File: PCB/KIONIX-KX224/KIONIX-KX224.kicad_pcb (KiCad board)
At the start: 2 copper layers, 7 parts, among them J1 Conn_02x03_Odd_Even

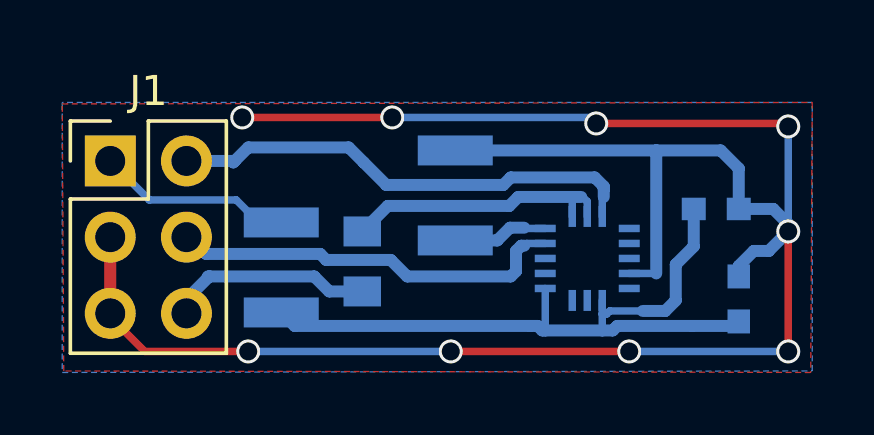
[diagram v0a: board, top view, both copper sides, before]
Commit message: PCB - KX224 update to have file conform to manufacturate PCB
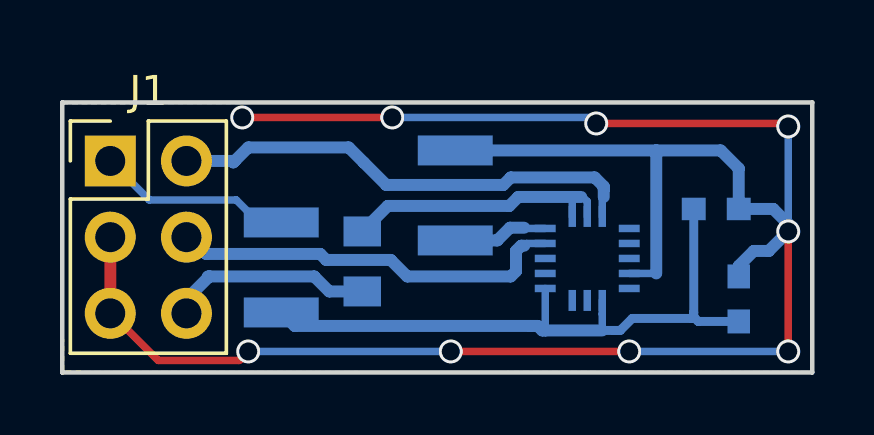
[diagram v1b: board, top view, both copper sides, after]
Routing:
- net /VDD: track 24.7 -> 22.7 mm
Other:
- board outline added: 25 x 9 mm
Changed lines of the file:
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@@
     (area 114.214287 82.025 152.200002 102.675)
     (thickness 1.6)
-    (drawings 6)
-    (tracks 114)
+    (drawings 26)
+    (tracks 115)
     (zones 0)
     (modules 7)
@@
     (pad_to_mask_clearance 0.2)
     (aux_axis_origin 0 0)
-    (visible_elements 7FFFF73F)
+    (visible_elements 7FFFF71F)
     (pcbplotparams
-      (layerselection 0x000cc_80000001)
+      (layerselection 0x000c4_80000001)
       (usegerberextensions false)
-      (excludeedgelayer false)
+      (usegerberattributes true)
+      (excludeedgelayer true)
       (linewidth 0.100000)
       (plotframeref false)
@@
       (effects (font (size 1 1) (thickness 0.15)) (justify mirror))
     )
-    (fp_text value KX224 (at -0.25 6.4) (layer B.Fab)
+    (fp_text value KX224 (at -0.25 6.4) (layer B.Fab) hide
       (effects (font (size 1 1) (thickness 0.15)) (justify mirror))
     )
@@
     )
   )
+  (gr_line (start 127 99) (end 127 90) (angle 90) (layer B.Mask) (width 0.2))
+  (gr_line (start 152 99) (end 127 99) (angle 90) (layer B.Mask) (width 0.2))
+  (gr_line (start 152 90) (end 152 99) (angle 90) (layer B.Mask) (width 0.2))
+  (gr_line (start 127 90) (end 152 90) (angle 90) (layer B.Mask) (width 0.2))
+  (gr_line (start 127 99) (end 127 90) (angle 90) (layer F.Mask) (width 0.2))
+  (gr_line (start 152 99) (end 127 99) (angle 90) (layer F.Mask) (width 0.2))
+  (gr_line (start 152 90) (end 152 99) (angle 90) (layer F.Mask) (width 0.2))
+  (gr_line (start 127 90) (end 152 90) (angle 90) (layer F.Mask) (width 0.2))
+  (gr_line (start 127 99) (end 127 90) (angle 90) (layer F.Mask) (width 0.2))
+  (gr_line (start 152 99) (end 127 99) (angle 90) (layer F.Mask) (width 0.2))
+  (gr_line (start 152 90) (end 152 99) (angle 90) (layer F.Mask) (width 0.2))
+  (gr_line (start 127 90) (end 152 90) (angle 90) (layer F.Mask) (width 0.2))
+  (gr_line (start 127 99) (end 127 90) (angle 90) (layer B.Paste) (width 0.2))
+  (gr_line (start 152 99) (end 127 99) (angle 90) (layer B.Paste) (width 0.2))
+  (gr_line (start 152 90) (end 152 99) (angle 90) (layer B.Paste) (width 0.2))
+  (gr_line (start 127 90) (end 152 90) (angle 90) (layer B.Paste) (width 0.2))
+  (gr_line (start 127 99) (end 127 90) (angle 90) (layer Edge.Cuts) (width 0.15))
+  (gr_line (start 152 99) (end 127 99) (angle 90) (layer Edge.Cuts) (width 0.15))
+  (gr_line (start 152 90) (end 152 99) (angle 90) (layer Edge.Cuts) (width 0.15))
+  (gr_line (start 127 90) (end 152 90) (angle 90) (layer Edge.Cuts) (width 0.15))
   (dimension 25 (width 0.3) (layer F.Fab)
     (gr_text "25,000 mm" (at 139.5 86.65) (layer F.Fab)
@@
   (gr_line (start 127 99) (end 152 99) (angle 90) (layer F.Fab) (width 0.2))
   (gr_line (start 127 90) (end 127 99) (angle 90) (layer F.Fab) (width 0.2))
+  (segment (start 128.6 97.03) (end 128.63 97.03) (width 0.25) (layer F.Cu) (net 1) (status C00000))
+  (segment (start 128.63 97.03) (end 130.2 98.6) (width 0.25) (layer F.Cu) (net 1) (status 400000))
+  (via (at 133.2 98.3) (size 0.8) (drill 0.6) (layers F.Cu B.Cu) (net 1))
+  (segment (start 133.2 98.3) (end 139.95 98.3) (width 0.25) (layer B.Cu) (net 1))
+  (via (at 139.95 98.3) (size 0.8) (drill 0.6) (layers F.Cu B.Cu) (net 1))
+  (segment (start 139.95 98.3) (end 145.9 98.3) (width 0.25) (layer F.Cu) (net 1))
+  (via (at 145.9 98.3) (size 0.8) (drill 0.6) (layers F.Cu B.Cu) (net 1))
+  (segment (start 145.9 98.3) (end 151.2 98.3) (width 0.25) (layer B.Cu) (net 1))
+  (via (at 151.2 98.3) (size 0.8) (drill 0.6) (layers F.Cu B.Cu) (net 1))
+  (segment (start 151.2 94.3) (end 151.2 98.3) (width 0.25) (layer F.Cu) (net 1))
+  (via (at 151.2 94.3) (size 0.8) (drill 0.6) (layers F.Cu B.Cu) (net 1))
+  (segment (start 132.9 98.6) (end 133.2 98.3) (width 0.25) (layer F.Cu) (net 1))
+  (segment (start 130.2 98.6) (end 132.9 98.6) (width 0.25) (layer F.Cu) (net 1))
+  (segment (start 128.6 97.03) (end 128.67 97.03) (width 0.2) (layer F.Cu) (net 1) (status C00000))
+  (segment (start 128.6 97.03) (end 128.6 97) (width 0.25) (layer F.Cu) (net 1))
   (segment (start 149.55 95.45) (end 150.05 94.95) (width 0.4) (layer B.Cu) (net 1) (status 10))
   (segment (start 150.55 94.95) (end 151.2 94.3) (width 0.4) (layer B.Cu) (net 1))
@@
   (segment (start 148.95 91.6) (end 149.55 92.2) (width 0.4) (layer B.Cu) (net 1))
   (segment (start 128.6 97.03) (end 128.6 94.49) (width 0.4) (layer F.Cu) (net 1))
-  (segment (start 133.2 98.3) (end 129.75 98.3) (width 0.25) (layer F.Cu) (net 1))
-  (via (at 133.2 98.3) (size 0.8) (drill 0.6) (layers F.Cu B.Cu) (net 1))
-  (segment (start 133.2 98.3) (end 139.95 98.3) (width 0.25) (layer B.Cu) (net 1))
-  (via (at 139.95 98.3) (size 0.8) (drill 0.6) (layers F.Cu B.Cu) (net 1))
-  (segment (start 139.95 98.3) (end 145.9 98.3) (width 0.25) (layer F.Cu) (net 1))
-  (via (at 145.9 98.3) (size 0.8) (drill 0.6) (layers F.Cu B.Cu) (net 1))
-  (segment (start 145.9 98.3) (end 151.2 98.3) (width 0.25) (layer B.Cu) (net 1))
-  (via (at 151.2 98.3) (size 0.8) (drill 0.6) (layers F.Cu B.Cu) (net 1))
-  (segment (start 151.2 94.3) (end 151.2 98.3) (width 0.25) (layer F.Cu) (net 1))
-  (via (at 151.2 94.3) (size 0.8) (drill 0.6) (layers F.Cu B.Cu) (net 1))
-  (segment (start 129.75 98.3) (end 128.6 97.15) (width 0.25) (layer F.Cu) (net 1))
   (segment (start 128.6 97.15) (end 128.6 97.03) (width 0.25) (layer F.Cu) (net 1))
   (segment (start 151.2 94.3) (end 151.2 90.8) (width 0.25) (layer B.Cu) (net 1))
@@
   (segment (start 151.2 94.05) (end 151.2 94.3) (width 0.4) (layer B.Cu) (net 1))
   (segment (start 149.55 93.55) (end 150.7 93.55) (width 0.4) (layer B.Cu) (net 1))
-  (segment (start 149.4 97.45) (end 148 97.45) (width 0.4) (layer B.Cu) (net 2) (status 10))
-  (segment (start 145.5 97.45) (end 148 97.45) (width 0.4) (layer B.Cu) (net 2))
-  (segment (start 145.35 97.6) (end 145.5 97.45) (width 0.4) (layer B.Cu) (net 2))
-  (segment (start 145.35 97.6) (end 145 97.6) (width 0.4) (layer B.Cu) (net 2))
+  (segment (start 145.4 97.6) (end 145.6 97.6) (width 0.3) (layer B.Cu) (net 2))
+  (segment (start 145 97.6) (end 145.4 97.6) (width 0.3) (layer B.Cu) (net 2))
+  (segment (start 148 97.2) (end 148.05 97.15) (width 0.3) (layer B.Cu) (net 2))
+  (segment (start 146 97.2) (end 148 97.2) (width 0.3) (layer B.Cu) (net 2))
+  (segment (start 145.6 97.6) (end 146 97.2) (width 0.3) (layer B.Cu) (net 2))
+  (segment (start 148.05 93.55) (end 148.05 97) (width 0.3) (layer B.Cu) (net 2))
+  (segment (start 148.05 97) (end 148.05 97.15) (width 0.3) (layer B.Cu) (net 2))
+  (segment (start 148.05 97.15) (end 148.2 97.3) (width 0.3) (layer B.Cu) (net 2))
+  (segment (start 148.2 97.3) (end 149.55 97.3) (width 0.3) (layer B.Cu) (net 2))
   (segment (start 149.4 97.45) (end 149.55 97.3) (width 0.4) (layer B.Cu) (net 2) (status 30))
-  (segment (start 148.05 94.8) (end 147.45 95.4) (width 0.4) (layer B.Cu) (net 2))
-  (segment (start 147.45 95.4) (end 147.45 96.6) (width 0.4) (layer B.Cu) (net 2))
-  (segment (start 147.45 96.6) (end 147.1 96.95) (width 0.4) (layer B.Cu) (net 2))
-  (segment (start 147.1 96.95) (end 146.35 96.95) (width 0.4) (layer B.Cu) (net 2))
-  (segment (start 148.05 94.8) (end 148.05 93.55) (width 0.4) (layer B.Cu) (net 2))
-  (segment (start 145.25 96.95) (end 146.35 96.95) (width 0.25) (layer B.Cu) (net 2))
-  (segment (start 145 97.05) (end 145.15 97.05) (width 0.25) (layer B.Cu) (net 2))
-  (segment (start 145.15 97.05) (end 145.25 96.95) (width 0.25) (layer B.Cu) (net 2))
   (segment (start 148.2 93.7) (end 148.05 93.55) (width 0.25) (layer B.Cu) (net 2))
   (segment (start 145 97.05) (end 145 97.6) (width 0.25) (layer B.Cu) (net 2))

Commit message: PCB - KX224 V2.0 verified
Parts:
- removed JP1: Jumper, Capacitors_SMD:C_0805
- removed JP2, JP3: Jumper, Capacitors_SMD:C_1210
- C1: footprint Capacitors_SMD:C_0603 -> Capacitors_SMD:C_0805; moved to F.Cu
- C2, Kx1: moved to F.Cu
- moved C1 8.65 mm to (140.2, 94.5), turned to 270 degrees
- moved C2 2.57 mm to (149.2, 94.0), turned to 270 degrees
- moved Kx1 1.35 mm to (145.4, 94.2)
- moved J1 0.30 mm to (128.9, 92.0)
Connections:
- J1 pad 1: Net-(J1-Pad1) -> /VDD
- J1 pad 6: Net-(J1-Pad6) -> /Miso/Mosi
- Kx1 pad 5: Net-(JP3-Pad2) -> GNDREF
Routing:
- net /CS/SCL: track 16.0 -> 31.1 mm
- net GNDREF: track 72.6 -> 62.6 mm, vias 9 -> 11
- net Net-(J1-Pad6): track 6.90 -> 0.00 mm
- net /Miso/Mosi: track 9.19 -> 15.9 mm
- net Net-(J1-Pad1): track 6.55 -> 0.00 mm
- net /VDD: track 22.7 -> 28.1 mm
- net Net-(JP3-Pad2): track 3.19 -> 0.00 mm
- net /SCLK: track 13.4 -> 12.6 mm
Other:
- board text added: "KX224 Eval Board CHAMP - October/2018"
- board text added: "Mosi Miso SCL"
- board text added: "SCLK"
- board text added: "VDD"

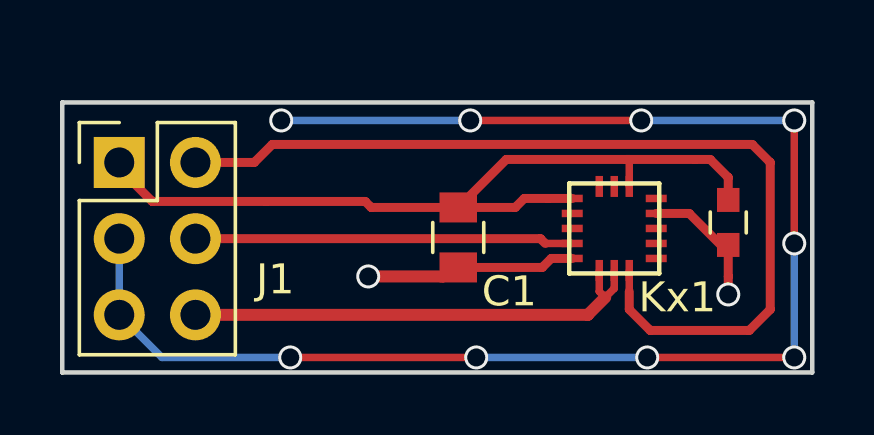
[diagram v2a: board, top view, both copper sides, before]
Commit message: PCB - kionix, fix pin wiring mistake
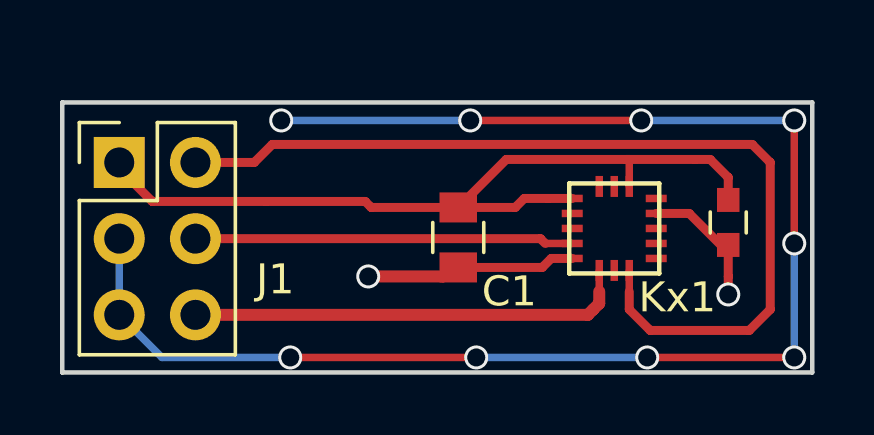
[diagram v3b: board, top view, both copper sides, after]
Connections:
- Kx1 pad 7: /Miso/Mosi -> Net-(Kx1-Pad7)
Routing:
- net /Miso/Mosi: track 15.9 -> 14.7 mm
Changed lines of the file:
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@@
 (kicad_pcb (version 4) (host pcbnew 4.0.7)
   (general
-    (links 13)
+    (links 12)
     (no_connects 0)
     (area 114.214287 82.7 163.785715 107.7)
     (thickness 1.6)
     (drawings 39)
-    (tracks 74)
+    (tracks 73)
     (zones 0)
     (modules 4)
-    (nets 14)
+    (nets 15)
   )
   (page A4)
@@
   )
   (setup
-    (last_trace_width 0.25)
+    (last_trace_width 0.4)
     (user_trace_width 0.2)
     (user_trace_width 0.3)
@@
     (visible_elements 7FFFF73F)
     (pcbplotparams
-      (layerselection 0x000cc_80000001)
+      (layerselection 0x00000_00000001)
       (usegerberextensions false)
       (excludeedgelayer true)
@@
   (net 12 "Net-(Kx1-Pad11)")
   (net 13 "Net-(Kx1-Pad10)")
+  (net 14 "Net-(Kx1-Pad7)")
   (net_class Default "Ceci est la Netclass par défaut"
     (clearance 0.2)
@@
     (add_net "Net-(Kx1-Pad2)")
     (add_net "Net-(Kx1-Pad3)")
+    (add_net "Net-(Kx1-Pad7)")
     (add_net "Net-(Kx1-Pad9)")
   )
@@
       (net 5 /Miso/Mosi))
     (pad 7 smd rect (at 0 1.4) (size 0.25 0.7) (layers F.Cu F.Paste F.Mask)
-      (net 5 /Miso/Mosi))
+      (net 14 "Net-(Kx1-Pad7)"))
     (pad 8 smd rect (at 0.5 1.4) (size 0.25 0.7) (layers F.Cu F.Paste F.Mask)
       (net 3 /CS/SCL))
@@
   (segment (start 143.1 94.7) (end 144 94.7) (width 0.25) (layer F.Cu) (net 4))
   (segment (start 142.94 94.54) (end 143.1 94.7) (width 0.3) (layer F.Cu) (net 4))
-  (segment (start 145.4 95.6) (end 145.4 96.2) (width 0.25) (layer F.Cu) (net 5))
-  (segment (start 145.4 96.2) (end 145.1 96.5) (width 0.25) (layer F.Cu) (net 5))
+  (segment (start 144.52 97.08) (end 144.7 96.9) (width 0.4) (layer F.Cu) (net 5))
   (segment (start 144.9 95.6) (end 144.9 96.3) (width 0.25) (layer F.Cu) (net 5))
-  (segment (start 144.52 97.08) (end 145.1 96.5) (width 0.4) (layer F.Cu) (net 5))
   (segment (start 144.52 97.08) (end 131.44 97.08) (width 0.4) (layer F.Cu) (net 5))
-  (segment (start 144.9 96.3) (end 145.1 96.5) (width 0.25) (layer F.Cu) (net 5))
+  (segment (start 144.9 96.7) (end 144.9 96.3) (width 0.4) (layer F.Cu) (net 5))
+  (segment (start 144.7 96.9) (end 144.9 96.7) (width 0.4) (layer F.Cu) (net 5))
   (zone (net 1) (net_name GNDREF) (layer F.Cu) (hatch edge 0.508)
     (connect_pads (clearance 0))
